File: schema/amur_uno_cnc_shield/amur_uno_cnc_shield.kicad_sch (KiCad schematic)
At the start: 26 parts, among them J1 Conn_01x04_Pin, J10 Conn_01x04_Pin, J11 Reset, J12 Conn_01x03_Pin, J13 Conn_01x01_Pin, J14 Conn_01x03_Pin, J15 Conn_01x03_Pin, J16 Conn_01x03_Pin, J2 Conn_01x04_Pin, J3 Conn_01x04_Pin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

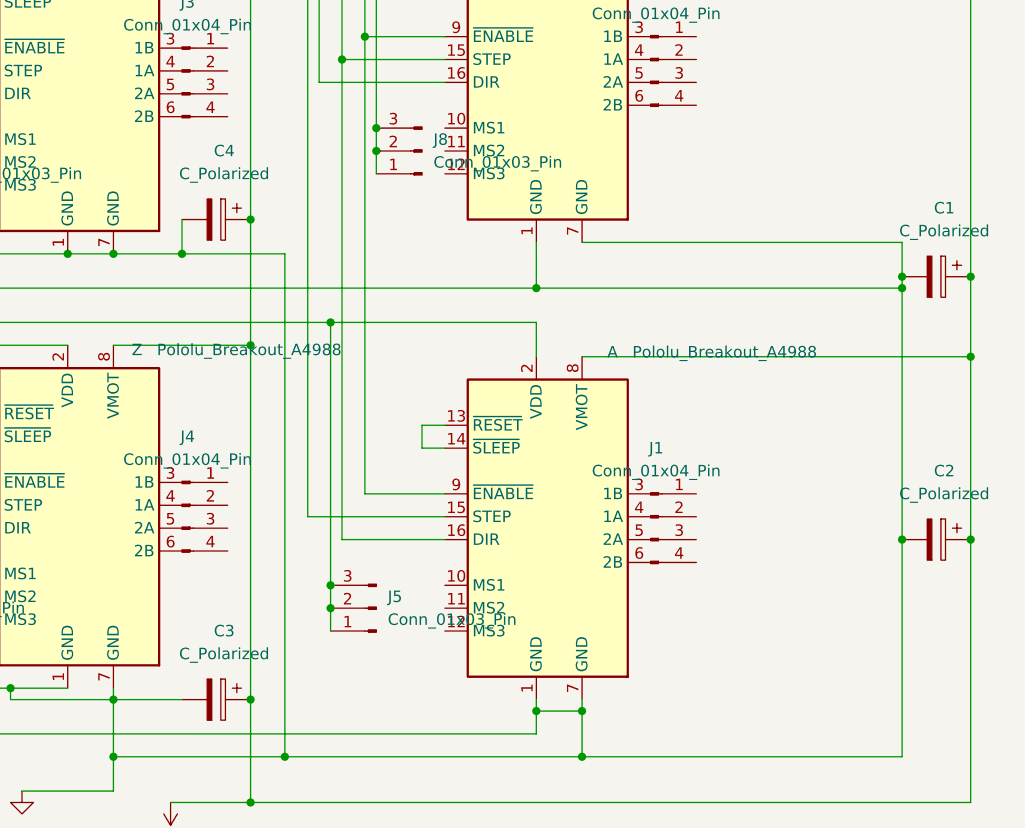
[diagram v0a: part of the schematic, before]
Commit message: Добавлены номеналы конденсаторов
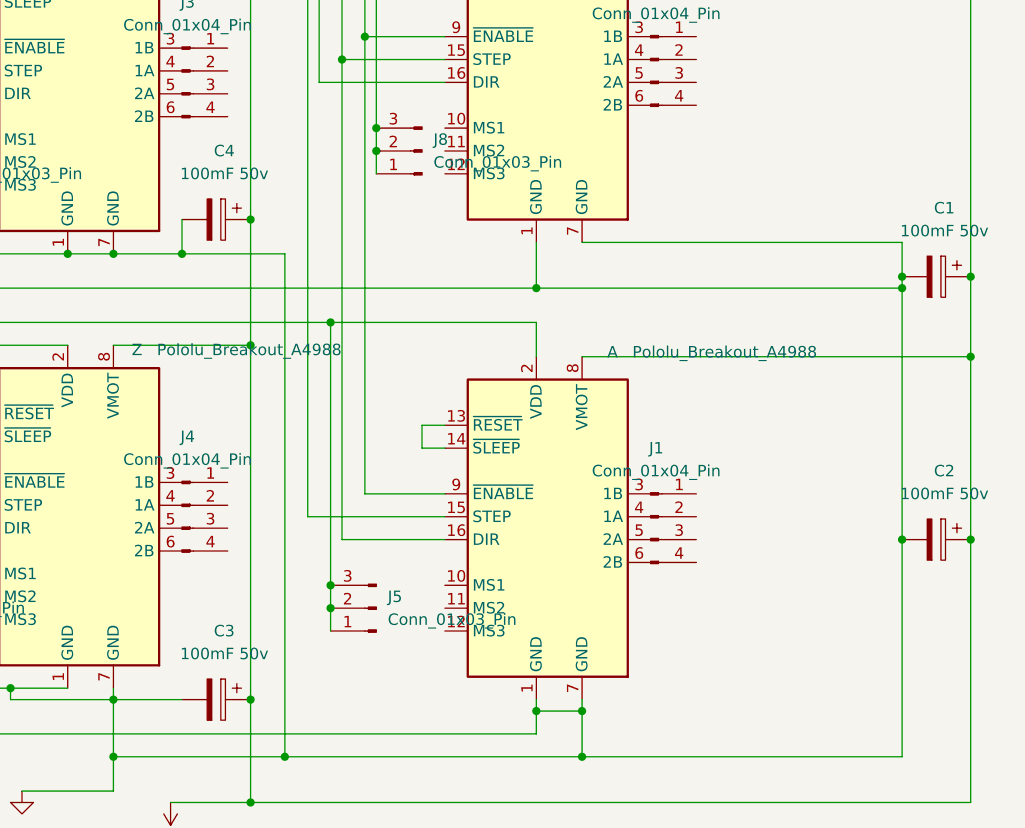
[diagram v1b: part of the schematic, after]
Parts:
- C1, C2, C3, C4: value C_Polarized -> 100mF 50v
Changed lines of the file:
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@@
 			)
 		)
-		(property "Value" "C_Polarized"
+		(property "Value" "100mF 50v"
 			(at 251.079 95.25 90)
 			(effects
@@
 			)
 		)
-		(property "Value" "C_Polarized"
+		(property "Value" "100mF 50v"
 			(at 251.079 66.04 90)
 			(effects
@@
 			)
 		)
-		(property "Value" "C_Polarized"
+		(property "Value" "100mF 50v"
 			(at 171.069 113.03 90)
 			(effects
@@
 			)
 		)
-		(property "Value" "C_Polarized"
+		(property "Value" "100mF 50v"
 			(at 171.069 59.69 90)
 			(effects

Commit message: Исправил схему
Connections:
- net at A.16 (DIR), ACE_UNO1.21 (А3_PORT_0.7): no longer ACE_UNO1.4 (D3_PORT_0.0_PWM_INT1_MISO(SPI0)), Y.15 (STEP)
- new net: ACE_UNO1.4 (D3_PORT_0.0_PWM_INT1_MISO(SPI0)), Y.15 (STEP)
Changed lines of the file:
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@@
-	)
-	(junction
-		(at 184.15 46.99)
-		(diameter 0)
-		(color 0 0 0 0)
 	)
 	(junction
@@
 	)
 	(junction
-		(at 184.15 20.32)
-		(diameter 0)
-		(color 0 0 0 0)
-	)
-	(junction
 		(at 186.69 44.45)
 		(diameter 0)
@@
 	(wire
 		(pts
-			(xy 184.15 46.99) (xy 195.58 46.99)
-		)
-		(stroke
-			(width 0)
-			(type default)
-		)
-	)
-	(wire
-		(pts
 			(xy 140.97 86.36) (xy 140.97 88.9)
 		)
@@
 	(wire
 		(pts
-			(xy 44.45 20.32) (xy 184.15 20.32)
-		)
-		(stroke
-			(width 0)
-			(type default)
-		)
-	)
-	(wire
-		(pts
 			(xy 48.26 38.1) (xy 48.26 22.86)
 		)
@@
 	(wire
 		(pts
-			(xy 184.15 15.24) (xy 184.15 20.32)
+			(xy 184.15 15.24) (xy 184.15 100.33)
 		)
 		(stroke
@@
 	(wire
 		(pts
+			(xy 177.8 20.32) (xy 177.8 46.99)
+		)
+		(stroke
+			(width 0)
+			(type default)
+		)
+	)
+	(wire
+		(pts
 			(xy 132.08 45.72) (xy 133.35 45.72)
 		)
@@
 	(wire
 		(pts
-			(xy 184.15 46.99) (xy 184.15 100.33)
-		)
-		(stroke
-			(width 0)
-			(type default)
-		)
-	)
-	(wire
-		(pts
 			(xy 210.82 29.21) (xy 210.82 24.13)
 		)
@@
 	(wire
 		(pts
+			(xy 177.8 46.99) (xy 195.58 46.99)
+		)
+		(stroke
+			(width 0)
+			(type default)
+		)
+	)
+	(wire
+		(pts
 			(xy 50.8 73.66) (xy 46.99 73.66)
 		)
@@
 	(wire
 		(pts
-			(xy 184.15 20.32) (xy 184.15 46.99)
-		)
-		(stroke
+			(xy 44.45 20.32) (xy 177.8 20.32)
+		)
+		(stroke
